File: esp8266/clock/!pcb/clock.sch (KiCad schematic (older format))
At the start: 7 parts, among them J1 Conn_01x05, J2 Conn_01x01, U1 WeMos_D1_mini, U2 rxb, U3 BME280

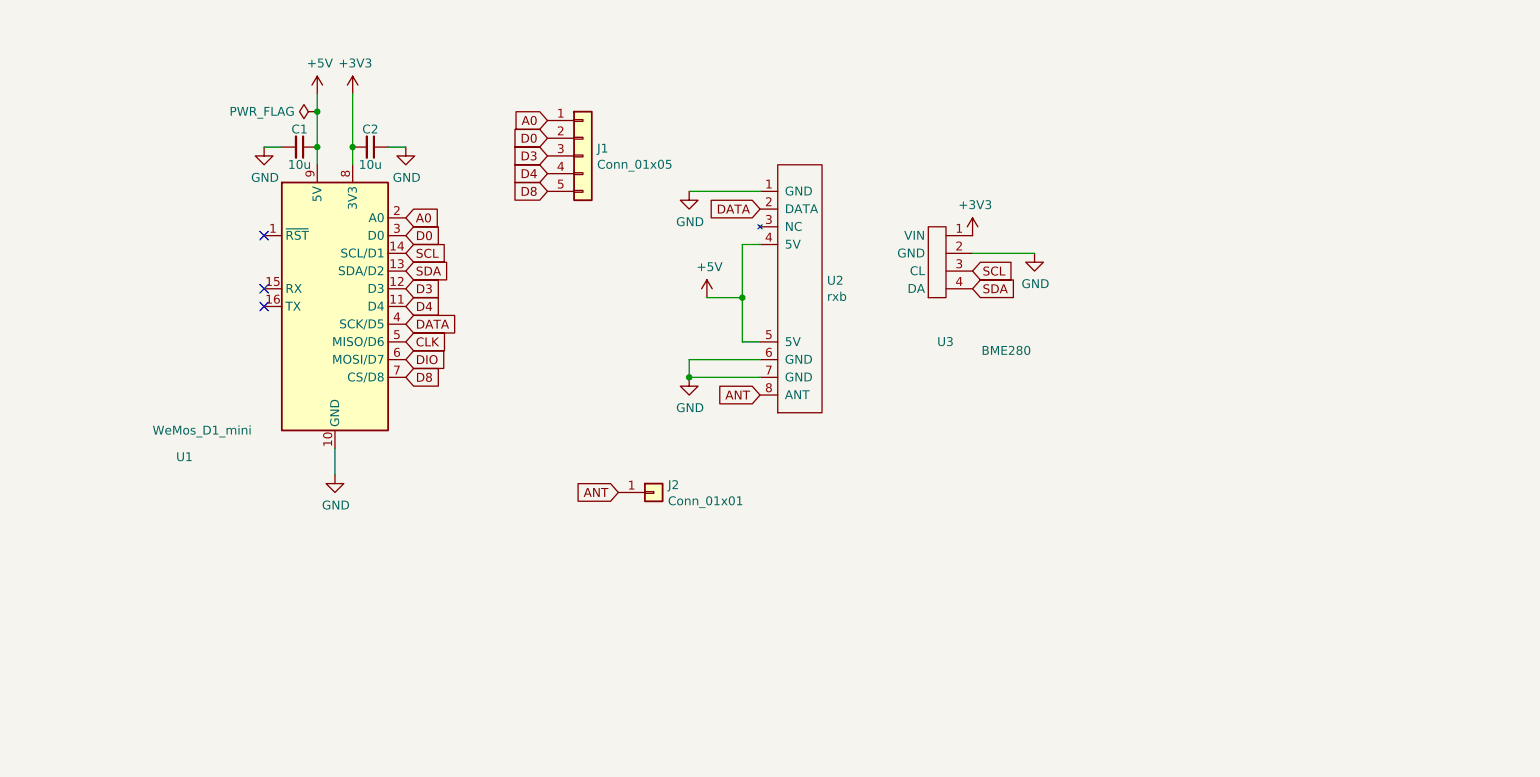
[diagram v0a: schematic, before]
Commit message: clock: Add more syms
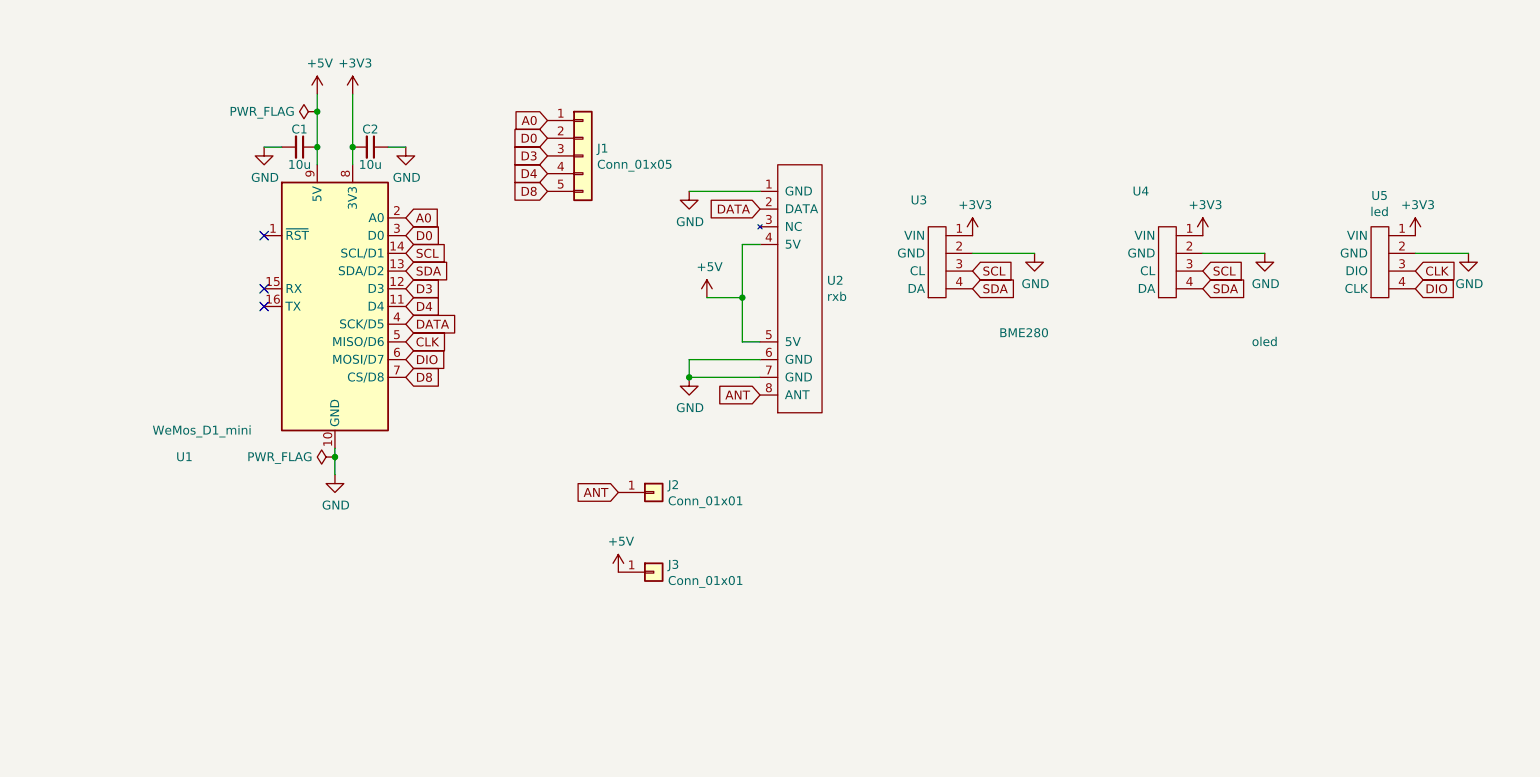
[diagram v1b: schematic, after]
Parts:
- added J3: Conn_01x01, symbol Connector_Generic:Conn_01x01
- added U4: oled, symbol !mysyms:oled
- added U5: led, symbol !mysyms:led
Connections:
- net +3V3: now also U4.1 (VIN), U5.1 (VIN)
- net +5V: now also J3.1 (Pin_1)
- net CLK: now also U5.3 (DIO)
- net DIO: now also U5.4 (CLK)
- net GND: now also U4.2 (GND), U5.2 (GND)
- net SCL: now also U4.3 (CL)
- net SDA: now also U4.4 (DA)
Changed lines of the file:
@@
 U 1 1 6016A9C6
 P 6150 2050
-F 0 "U3" V 6600 1900 50  0000 L CNN
-F 1 "BME280" V 6650 2150 50  0000 L CNN
+F 0 "U3" V 5800 1750 50  0000 L CNN
+F 1 "BME280" V 6550 2250 50  0000 L CNN
 F 2 "" V 6100 2150 50  0001 C CNN
 F 3 "" V 6100 2150 50  0001 C CNN
@@
 Wire Wire Line
 	2500 1100 2500 1200
-Wire Wire Line
-	2600 3100 2600 3250
 $Comp
 L Connector_Generic:Conn_01x05 J1
@@
 Wire Wire Line
 	2500 1200 2500 1400
+$Comp
+L !mysyms:oled U4
+U 1 1 6015EBC4
+P 7450 2050
+F 0 "U4" V 7050 1750 50  0000 C CNN
+F 1 "oled" V 7900 2450 50  0000 C CNN
+F 2 "" V 7400 2150 50  0001 C CNN
+F 3 "" V 7400 2150 50  0001 C CNN
+	1    7450 2050
+	0    1    1    0
+$EndComp
+$Comp
+L power:+3V3 #PWR01
+U 1 1 6015F7B7
+P 7500 1900
+F 0 "#PWR01" H 7500 1750 50  0001 C CNN
+F 1 "+3V3" H 7515 2073 50  0000 C CNN
+F 2 "" H 7500 1900 50  0001 C CNN
+F 3 "" H 7500 1900 50  0001 C CNN
+	1    7500 1900
+	1    0    0    -1
+$EndComp
+Text GLabel 7500 2100 2    50   Input ~ 0
+SCL
+Text GLabel 7500 2200 2    50   Input ~ 0
+SDA
+$Comp
+L power:GND #PWR02
+U 1 1 60160948
+P 7850 2000
+F 0 "#PWR02" H 7850 1750 50  0001 C CNN
+F 1 "GND" H 7855 1827 50  0000 C CNN
+F 2 "" H 7850 2000 50  0001 C CNN
+F 3 "" H 7850 2000 50  0001 C CNN
+	1    7850 2000
+	1    0    0    -1
+$EndComp
+Wire Wire Line
+	7850 2000 7500 2000
+Wire Wire Line
+	2600 3100 2600 3150
+$Comp
+L !mysyms:led U5
+U 1 1 60163EA9
+P 8650 2050
+F 0 "U5" V 8275 1898 50  0000 C CNN
+F 1 "led" V 8366 1898 50  0000 C CNN
+F 2 "" V 8600 2150 50  0001 C CNN
+F 3 "" V 8600 2150 50  0001 C CNN
+	1    8650 2050
+	0    1    1    0
+$EndComp
+$Comp
+L power:+3V3 #PWR04
+U 1 1 601661B6
+P 8700 1900
+F 0 "#PWR04" H 8700 1750 50  0001 C CNN
+F 1 "+3V3" H 8715 2073 50  0000 C CNN
+F 2 "" H 8700 1900 50  0001 C CNN
+F 3 "" H 8700 1900 50  0001 C CNN
+	1    8700 1900
+	1    0    0    -1
+$EndComp
+$Comp
+L power:GND #PWR05
+U 1 1 60166F3C
+P 9000 2000
+F 0 "#PWR05" H 9000 1750 50  0001 C CNN
+F 1 "GND" H 9005 1827 50  0000 C CNN
+F 2 "" H 9000 2000 50  0001 C CNN
+F 3 "" H 9000 2000 50  0001 C CNN
+	1    9000 2000
+	1    0    0    -1
+$EndComp
+Wire Wire Line
+	8700 2000 9000 2000
+Text GLabel 8700 2100 2    50   Input ~ 0
+CLK
+Text GLabel 8700 2200 2    50   Input ~ 0
+DIO
+$Comp
+L Connector_Generic:Conn_01x01 J3
+U 1 1 6016876C
+P 4400 3800
+F 0 "J3" H 4480 3842 50  0000 L CNN
+F 1 "Conn_01x01" H 4480 3751 50  0000 L CNN
+F 2 "" H 4400 3800 50  0001 C CNN
+F 3 "~" H 4400 3800 50  0001 C CNN
+	1    4400 3800
+	1    0    0    -1
+$EndComp
+$Comp
+L power:+5V #PWR03
+U 1 1 6016910D
+P 4200 3800
+F 0 "#PWR03" H 4200 3650 50  0001 C CNN
+F 1 "+5V" H 4215 3973 50  0000 C CNN
+F 2 "" H 4200 3800 50  0001 C CNN
+F 3 "" H 4200 3800 50  0001 C CNN
+	1    4200 3800
+	1    0    0    -1
+$EndComp
+$Comp
+L power:PWR_FLAG #FLG0102
+U 1 1 6016A863
+P 2600 3150
+F 0 "#FLG0102" H 2600 3225 50  0001 C CNN
+F 1 "PWR_FLAG" V 2600 3277 50  0000 L CNN
+F 2 "" H 2600 3150 50  0001 C CNN
+F 3 "~" H 2600 3150 50  0001 C CNN
+	1    2600 3150
+	0    -1   -1   0
+$EndComp
+Connection ~ 2600 3150
+Wire Wire Line
+	2600 3150 2600 3250
 $EndSCHEMATC

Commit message: clock: Start routing
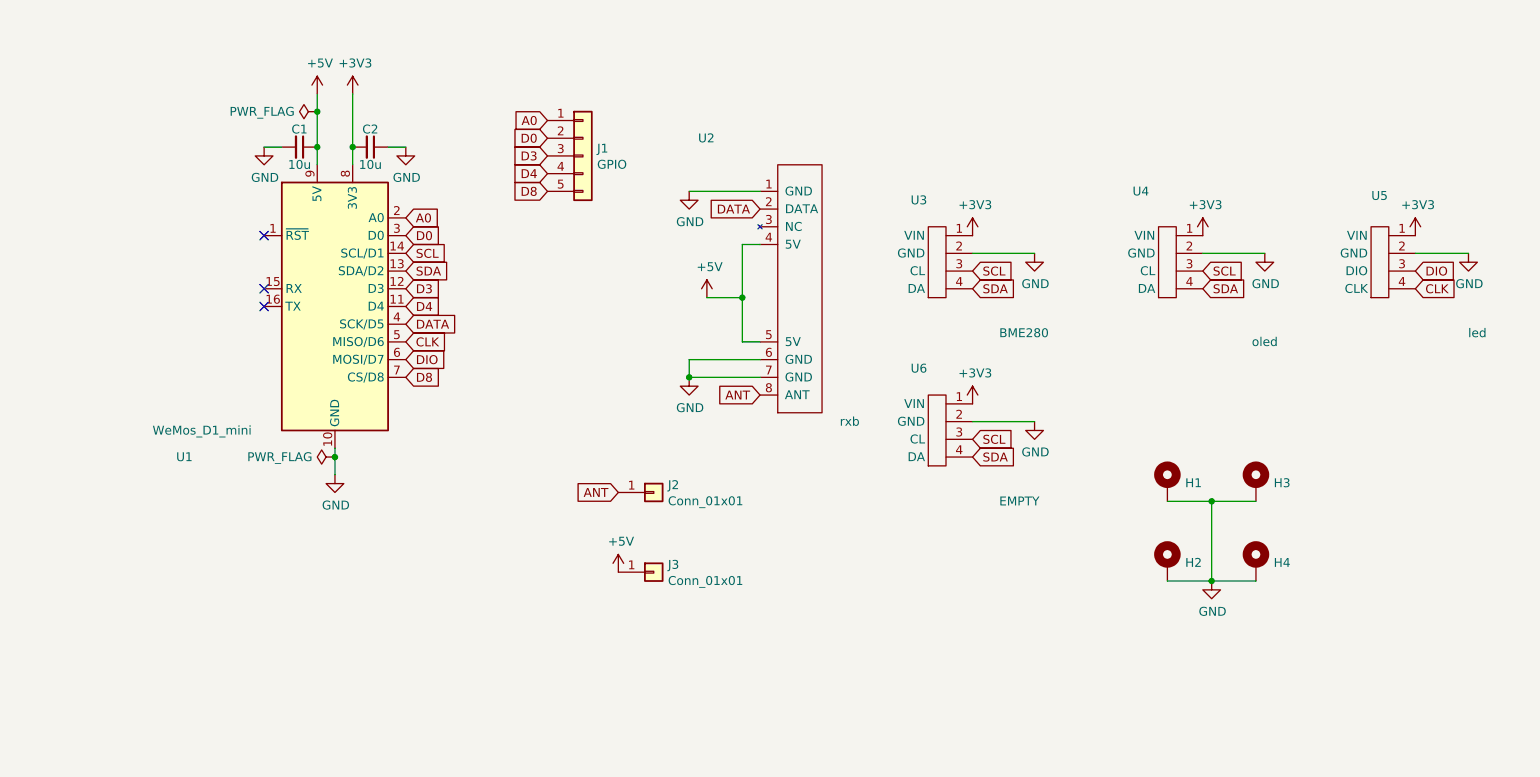
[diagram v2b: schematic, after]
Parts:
- added H1, H2, H3, H4: MountingHole_Pad, MountingHole:MountingHole_2.2mm_M2_Pad, symbol Mechanical:MountingHole_Pad
- added U6: EMPTY, !myfoots:4pinI2C, symbol !mysyms:bme280pbc
- C1, C2: footprint (none) -> Capacitor_SMD:C_0805_2012Metric_Pad1.18x1.45mm_HandSolder
- J1: value Conn_01x05 -> GPIO; footprint (none) -> Connector_PinHeader_2.54mm:PinHeader_1x05_P2.54mm_Vertical
- J2, J3: footprint (none) -> Connector_PinHeader_2.54mm:PinHeader_1x01_P2.54mm_Vertical
- U2: footprint (none) -> !myfoots:rxb
- U3, U4: footprint (none) -> !myfoots:4pinI2C
- U5: footprint (none) -> !myfoots:4pinTM1637
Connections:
- net +3V3: now also U6.1 (VIN)
- net CLK: now also U5.4 (CLK); no longer U5.3 (DIO)
- net DIO: now also U5.3 (DIO); no longer U5.4 (CLK)
- net GND: now also H1.1, H2.1, H3.1, H4.1, U6.2 (GND)
- net SCL: now also U6.3 (CL)
- net SDA: now also U6.4 (DA)
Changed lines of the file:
@@
 F 0 "C1" V 2300 1400 50  0000 C CNN
 F 1 "10u" V 2500 1400 50  0000 C CNN
-F 2 "" H 2400 1400 50  0001 C CNN
+F 2 "Capacitor_SMD:C_0805_2012Metric_Pad1.18x1.45mm_HandSolder" H 2400 1400 50  0001 C CNN
 F 3 "~" H 2400 1400 50  0001 C CNN
 	1    2400 1400
@@
 F 0 "C2" V 2700 1400 50  0000 C CNN
 F 1 "10u" V 2900 1400 50  0000 C CNN
-F 2 "" H 2800 1400 50  0001 C CNN
+F 2 "Capacitor_SMD:C_0805_2012Metric_Pad1.18x1.45mm_HandSolder" H 2800 1400 50  0001 C CNN
 F 3 "~" H 2800 1400 50  0001 C CNN
 	1    2800 1400
@@
 U 1 1 601603AC
 P 5150 2250
-F 0 "U2" V 5054 2478 50  0000 L CNN
-F 1 "rxb" V 5145 2478 50  0000 L CNN
-F 2 "" H 5150 2100 50  0001 C CNN
+F 0 "U2" V 4250 1750 50  0000 L CNN
+F 1 "rxb" V 5850 2550 50  0000 L CNN
+F 2 "!myfoots:rxb" H 5150 2100 50  0001 C CNN
 F 3 "" H 5150 2100 50  0001 C CNN
 	1    5150 2250
@@
 F 0 "U3" V 5800 1750 50  0000 L CNN
 F 1 "BME280" V 6550 2250 50  0000 L CNN
-F 2 "" V 6100 2150 50  0001 C CNN
+F 2 "!myfoots:4pinI2C" V 6100 2150 50  0001 C CNN
 F 3 "" V 6100 2150 50  0001 C CNN
 	1    6150 2050
@@
 P 4000 1450
 F 0 "J1" H 4080 1492 50  0000 L CNN
-F 1 "Conn_01x05" H 4080 1401 50  0000 L CNN
-F 2 "" H 4000 1450 50  0001 C CNN
+F 1 "GPIO" H 4080 1401 50  0000 L CNN
+F 2 "Connector_PinHeader_2.54mm:PinHeader_1x05_P2.54mm_Vertical" H 4000 1450 50  0001 C CNN
 F 3 "~" H 4000 1450 50  0001 C CNN
 	1    4000 1450
@@
 F 0 "J2" H 4480 3392 50  0000 L CNN
 F 1 "Conn_01x01" H 4480 3301 50  0000 L CNN
-F 2 "" H 4400 3350 50  0001 C CNN
+F 2 "Connector_PinHeader_2.54mm:PinHeader_1x01_P2.54mm_Vertical" H 4400 3350 50  0001 C CNN
 F 3 "~" H 4400 3350 50  0001 C CNN
 	1    4400 3350
@@
 F 0 "U4" V 7050 1750 50  0000 C CNN
 F 1 "oled" V 7900 2450 50  0000 C CNN
-F 2 "" V 7400 2150 50  0001 C CNN
+F 2 "!myfoots:4pinI2C" V 7400 2150 50  0001 C CNN
 F 3 "" V 7400 2150 50  0001 C CNN
 	1    7450 2050
@@
 P 8650 2050
 F 0 "U5" V 8275 1898 50  0000 C CNN
-F 1 "led" V 8366 1898 50  0000 C CNN
-F 2 "" V 8600 2150 50  0001 C CNN
+F 1 "led" V 9050 2450 50  0000 C CNN
+F 2 "!myfoots:4pinTM1637" V 8600 2150 50  0001 C CNN
 F 3 "" V 8600 2150 50  0001 C CNN
 	1    8650 2050
@@
 Wire Wire Line
 	8700 2000 9000 2000
+Text GLabel 8700 2200 2    50   Input ~ 0
+CLK
 Text GLabel 8700 2100 2    50   Input ~ 0
-CLK
-Text GLabel 8700 2200 2    50   Input ~ 0
 DIO
 $Comp
@@
 F 0 "J3" H 4480 3842 50  0000 L CNN
 F 1 "Conn_01x01" H 4480 3751 50  0000 L CNN
-F 2 "" H 4400 3800 50  0001 C CNN
+F 2 "Connector_PinHeader_2.54mm:PinHeader_1x01_P2.54mm_Vertical" H 4400 3800 50  0001 C CNN
 F 3 "~" H 4400 3800 50  0001 C CNN
 	1    4400 3800
@@
 Wire Wire Line
 	2600 3150 2600 3250
+$Comp
+L Mechanical:MountingHole_Pad H1
+U 1 1 60169893
+P 7300 3300
+F 0 "H1" H 7400 3303 50  0000 L CNN
+F 1 "MountingHole_Pad" H 7400 3258 50  0001 L CNN
+F 2 "MountingHole:MountingHole_2.2mm_M2_Pad" H 7300 3300 50  0001 C CNN
+F 3 "~" H 7300 3300 50  0001 C CNN
+	1    7300 3300
+	1    0    0    -1
+$EndComp
+$Comp
+L Mechanical:MountingHole_Pad H3
+U 1 1 6016A8E6
+P 7800 3300
+F 0 "H3" H 7900 3303 50  0000 L CNN
+F 1 "MountingHole_Pad" H 7900 3258 50  0001 L CNN
+F 2 "MountingHole:MountingHole_2.2mm_M2_Pad" H 7800 3300 50  0001 C CNN
+F 3 "~" H 7800 3300 50  0001 C CNN
+	1    7800 3300
+	1    0    0    -1
+$EndComp
+$Comp
+L Mechanical:MountingHole_Pad H2
+U 1 1 6016ADFE
+P 7300 3750
+F 0 "H2" H 7400 3753 50  0000 L CNN
+F 1 "MountingHole_Pad" H 7400 3708 50  0001 L CNN
+F 2 "MountingHole:MountingHole_2.2mm_M2_Pad" H 7300 3750 50  0001 C CNN
+F 3 "~" H 7300 3750 50  0001 C CNN
+	1    7300 3750
+	1    0    0    -1
+$EndComp
+$Comp
+L Mechanical:MountingHole_Pad H4
+U 1 1 6016B18D
+P 7800 3750
+F 0 "H4" H 7900 3753 50  0000 L CNN
+F 1 "MountingHole_Pad" H 7900 3708 50  0001 L CNN
+F 2 "MountingHole:MountingHole_2.2mm_M2_Pad" H 7800 3750 50  0001 C CNN
+F 3 "~" H 7800 3750 50  0001 C CNN
+	1    7800 3750
+	1    0    0    -1
+$EndComp
+Wire Wire Line
+	7300 3400 7550 3400
+Wire Wire Line
+	7550 3400 7550 3850
+Wire Wire Line
+	7550 3850 7800 3850
+Connection ~ 7550 3400
+Wire Wire Line
+	7550 3400 7800 3400
+Wire Wire Line
+	7300 3850 7550 3850
+Connection ~ 7550 3850
+$Comp
+L power:GND #PWR06
+U 1 1 6016C9D5
+P 7550 3850
+F 0 "#PWR06" H 7550 3600 50  0001 C CNN
+F 1 "GND" H 7555 3677 50  0000 C CNN
+F 2 "" H 7550 3850 50  0001 C CNN
+F 3 "" H 7550 3850 50  0001 C CNN
+	1    7550 3850
+	1    0    0    -1
+$EndComp
+$Comp
+L !mysyms:bme280pbc U6
+U 1 1 6017FC57
+P 6150 3000
+F 0 "U6" V 5800 2700 50  0000 L CNN
+F 1 "EMPTY" V 6550 3200 50  0000 L CNN
+F 2 "!myfoots:4pinI2C" V 6100 3100 50  0001 C CNN
+F 3 "" V 6100 3100 50  0001 C CNN
+	1    6150 3000
+	0    1    1    0
+$EndComp
+$Comp
+L power:+3V3 #PWR07
+U 1 1 6017FC5D
+P 6200 2850
+F 0 "#PWR07" H 6200 2700 50  0001 C CNN
+F 1 "+3V3" H 6215 3023 50  0000 C CNN
+F 2 "" H 6200 2850 50  0001 C CNN
+F 3 "" H 6200 2850 50  0001 C CNN
+	1    6200 2850
+	1    0    0    -1
+$EndComp
+$Comp
+L power:GND #PWR08
+U 1 1 6017FC63
+P 6550 2950
+F 0 "#PWR08" H 6550 2700 50  0001 C CNN
+F 1 "GND" H 6555 2777 50  0000 C CNN
+F 2 "" H 6550 2950 50  0001 C CNN
+F 3 "" H 6550 2950 50  0001 C CNN
+	1    6550 2950
+	1    0    0    -1
+$EndComp
+Text GLabel 6200 3050 2    50   Input ~ 0
+SCL
+Wire Wire Line
+	6200 2950 6550 2950
+Text GLabel 6200 3150 2    50   Input ~ 0
+SDA
 $EndSCHEMATC

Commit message: clock: Start routing
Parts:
- J3: footprint Connector_PinHeader_2.54mm:PinHeader_1x01_P2.54mm_Vertical -> Connector_PinHeader_2.54mm:PinHeader_1x02_P2.54mm_Vertical; symbol Connector_Generic:Conn_01x01 -> Connector_Generic:Conn_01x02
- U2: value rxb -> RXB6
- U4: value oled -> OLED
- U5: value led -> LED
- U6: value EMPTY -> SPARE
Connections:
- net +5V: now also J3.2 (Pin_2)
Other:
- moved on the sheet: C1, C2, H1, H2, H3, H4, J1, J2, U1, U2, U3, U4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

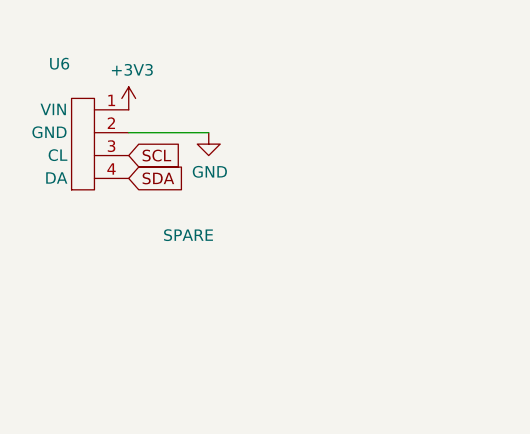
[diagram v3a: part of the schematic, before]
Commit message: clock: Send v10 to fab
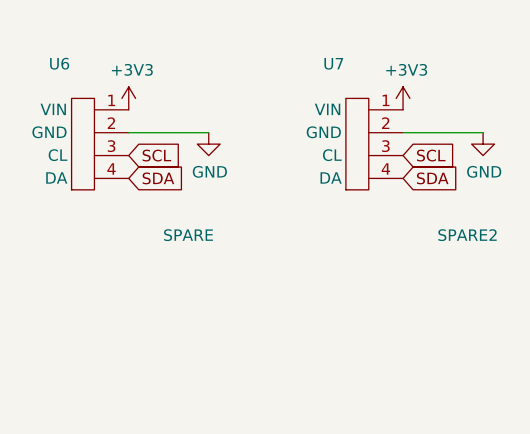
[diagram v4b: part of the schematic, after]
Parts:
- added U7: SPARE2, !myfoots:4pinI2C, symbol !mysyms:bme280pbc
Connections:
- net +3V3: now also U7.1 (VIN)
- net GND: now also U7.2 (GND)
- net SCL: now also U7.3 (CL)
- net SDA: now also U7.4 (DA)
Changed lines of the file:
@@
 	2900 4300 2900 4200
 Connection ~ 2900 4200
+$Comp
+L !mysyms:bme280pbc U7
+U 1 1 60193573
+P 8800 1200
+F 0 "U7" V 8450 900 50  0000 L CNN
+F 1 "SPARE2" V 9200 1400 50  0000 L CNN
+F 2 "!myfoots:4pinI2C" V 8750 1300 50  0001 C CNN
+F 3 "" V 8750 1300 50  0001 C CNN
+	1    8800 1200
+	0    1    1    0
+$EndComp
+$Comp
+L power:+3V3 #PWR09
+U 1 1 601937DF
+P 8850 1050
+F 0 "#PWR09" H 8850 900 50  0001 C CNN
+F 1 "+3V3" H 8865 1223 50  0000 C CNN
+F 2 "" H 8850 1050 50  0001 C CNN
+F 3 "" H 8850 1050 50  0001 C CNN
+	1    8850 1050
+	1    0    0    -1
+$EndComp
+$Comp
+L power:GND #PWR010
+U 1 1 601937E9
+P 9200 1150
+F 0 "#PWR010" H 9200 900 50  0001 C CNN
+F 1 "GND" H 9205 977 50  0000 C CNN
+F 2 "" H 9200 1150 50  0001 C CNN
+F 3 "" H 9200 1150 50  0001 C CNN
+	1    9200 1150
+	1    0    0    -1
+$EndComp
+Text GLabel 8850 1250 2    50   Input ~ 0
+SCL
+Wire Wire Line
+	8850 1150 9200 1150
+Text GLabel 8850 1350 2    50   Input ~ 0
+SDA
 $EndSCHEMATC
